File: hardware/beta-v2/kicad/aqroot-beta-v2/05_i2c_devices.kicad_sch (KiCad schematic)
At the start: 9 parts, among them U4 BMI270

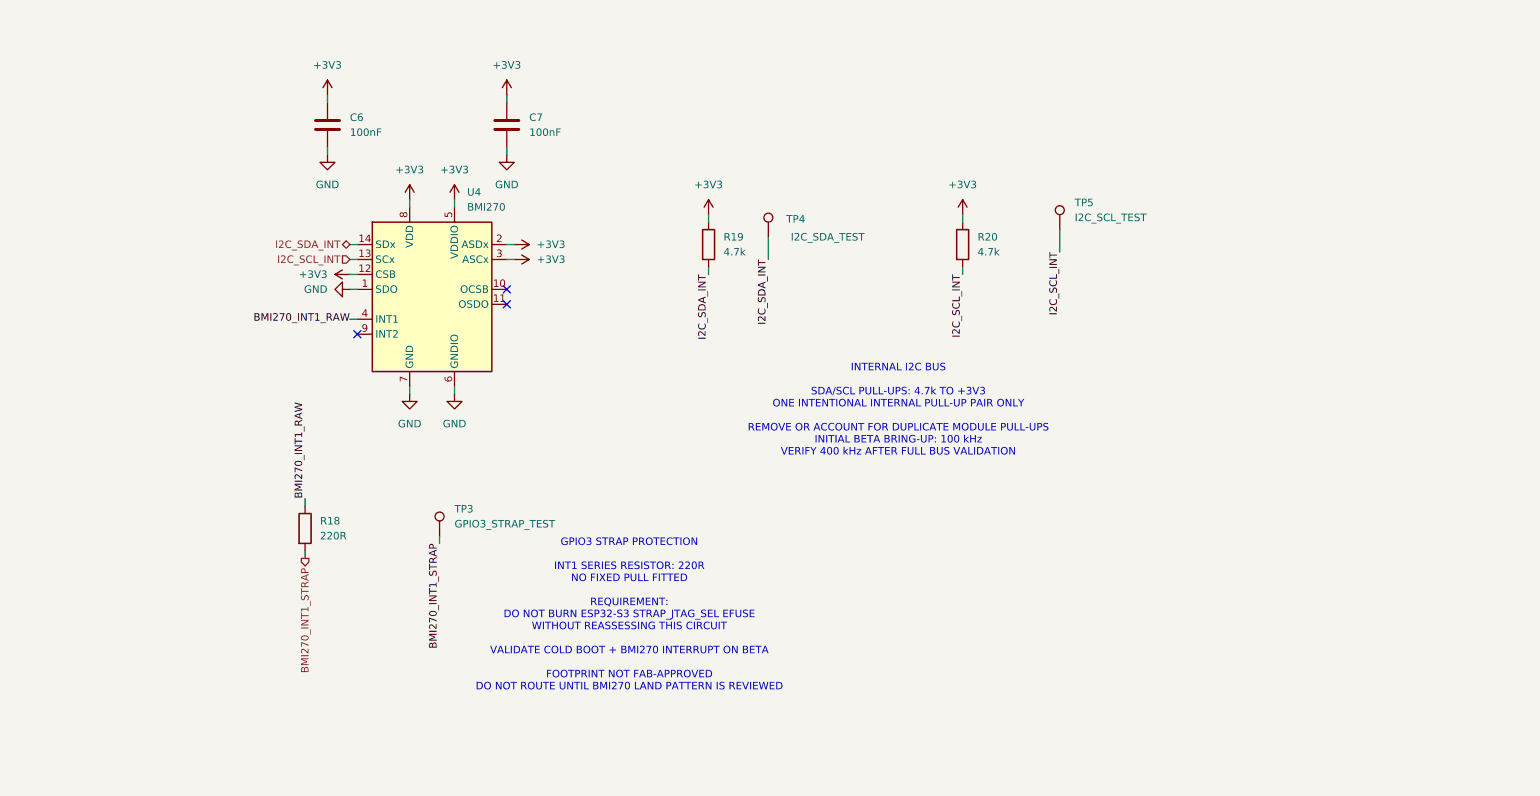
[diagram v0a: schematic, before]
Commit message: hardware: migrate Full Beta v2 I2C devices and IMU (FBV2-S1-005)
Sheet 05. Task gate FBV2-S1-I2C-IMU = PASS.
ERC 46 -> 45: zero added, one removed. Errors remain 2, both inherited.

A REPORTED NUMBER HAD TO BE CORRECTED FIRST.

FBV2-S1-004, 004B and 004C all quote "ERC 68". The stored reports say 46 -
2 errors, 44 warnings, three times over. The deltas those tasks reported
("zero added, zero removed") are correct and reproducible from the files; only
the absolute figure was wrong, and it was carried for three tasks. Sheet 04's
migration genuinely took the count from 64 to 46.

There is also a flag trap worth writing down: kicad-cli sch erc --severity-all
counts Exclusions as well and reports 104 on the same unmodified design. Every
figure in this programme is --severity-error --severity-warning, matching the
reports' own "Report includes: Errors, Warnings" header. Compare like with like
or the gate is meaningless.

NOTHING ON THIS SHEET WAS WRONG, AND THAT IS THE HONEST HEADLINE.

The brief said not to copy Beta-DM's BMI270 straps blindly. Every one was
re-derived from BST-BMI270-DS000-08 Rev 1.6:

  pin 1  SDO  -> GND    "the default I2C address ... 0b1101000 (0x68) ... if
                        the SDO pin is pulled to GND"
  pin 12 CSB  -> VDDIO  "it is recommended to hard-wire the CSB line to VDDIO"
  pin 2  ASDx -> VDDIO  "can be connected to VDDIO or left unconnected.
  pin 3  ASCx -> VDDIO   Do not connect to GND."
  pin 9  INT2 -> DNC    "If INT1 and/or INT2 are not used, please do not
  pin 10 OCSB -> DNC     connect them (DNC)."
  pin 11 OSDO -> DNC
  C6/C7 100nF at pins 5 and 8, exactly as recommended

They were all already correct. B-44 CLOSED: pad drive is IOH/IOL <= 2 mA with
VOH >= 0.8*VDDIO, against a 323 uA load - 6x margin.

THE REAL DEFECT WAS ON THE BUS.

The internal I2C bus was measured from the netlist rather than assumed - two
expanders, the IMU, the fuel gauge, the TCA9517A A-side, the touch controller
through the 50-pin display flex, two t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
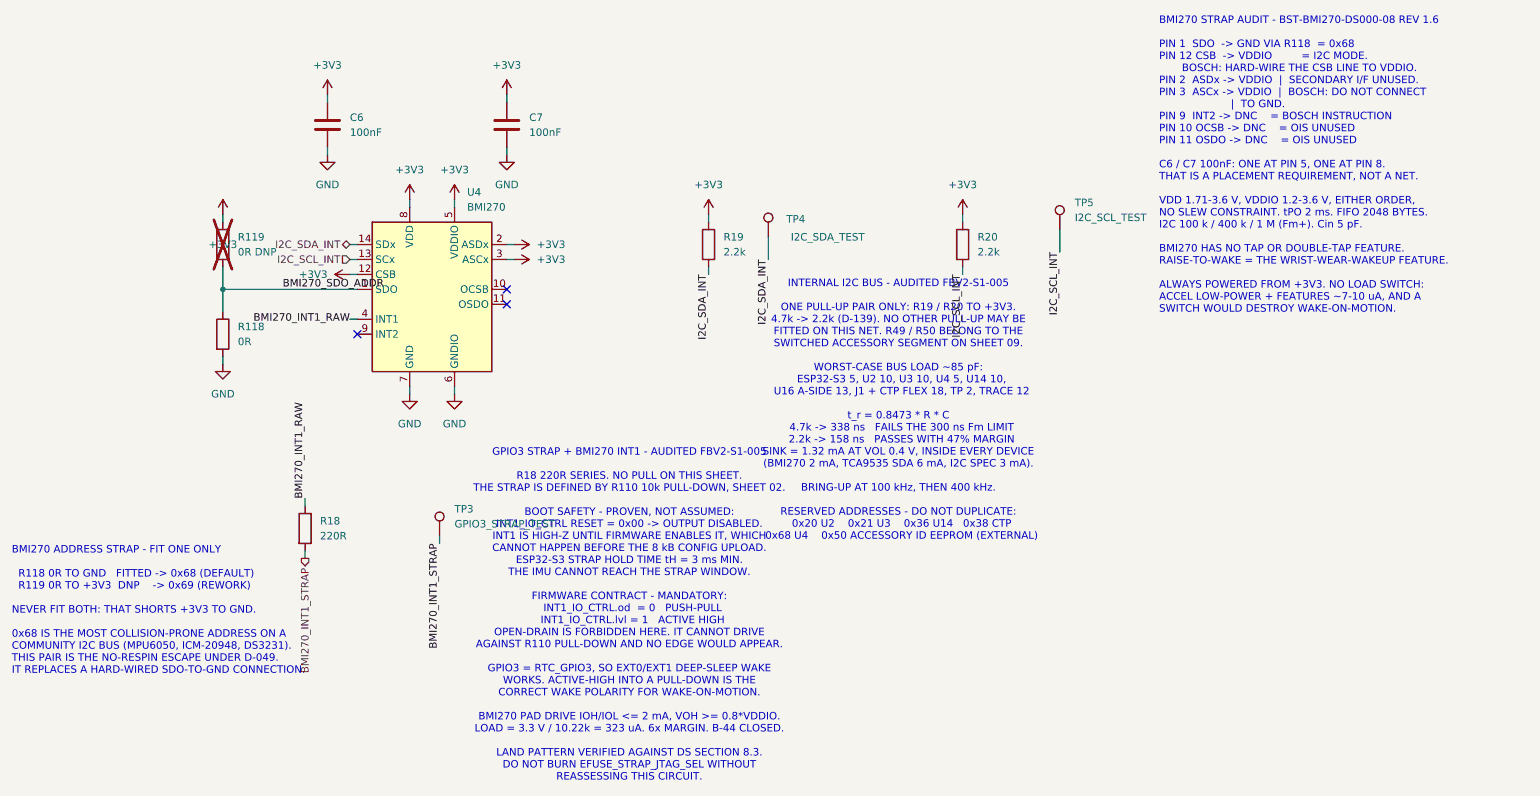
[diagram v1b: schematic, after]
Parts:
- added R118: 0R, Resistor_SMD:R_0603_1608Metric, symbol Device:R
- added R119: 0R DNP, Resistor_SMD:R_0603_1608Metric, symbol Device:R
- R19, R20: value 4.7k -> 2.2k
- U4: Note (none) -> Verified against BST-BMI270-DS000-08 Rev 1.6 (March 2026) i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
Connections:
- net +3V3: now also R119.1
- net GND: now also R118.2; no longer U4.1 (SDO)
- new net BMI270_SDO_ADDR: R118.1, R119.2, U4.1 (SDO)
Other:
- note added: "BMI270 ADDRESS STRAP - FIT ONE ONLY R118 0R TO GND FITTED -> 0x68 (DEFAULT) R119 0R TO +3V3 DNP -> 0x69 (REWORK) NEVER FIT BOTH: THAT SHORTS +3V3 TO GND. 0x68 IS THE MOST COLLISION-PRONE ADDRESS ON A COMMUNITY I2C BUS (MPU6050, ICM-20948, DS3231). THIS PAIR IS THE NO-RESPIN ESCAPE UNDER D-049. IT REPLACES A HARD-WIRED SDO-TO-GND CONNECTION."
- note added: "BMI270 STRAP AUDIT - BST-BMI270-DS000-08 REV 1.6 PIN 1 SDO -> GND VIA R118 = 0x68 PIN 12 CSB -> VDDIO = I2C MODE. BOSCH: HARD-WIRE THE CSB LINE TO VDDIO. PIN 2 ASDx -> VDDIO | SECONDARY I/F UNUSED. PIN 3 ASCx -> VDDIO | BOSCH: DO NOT CONNECT | TO GND. PIN 9 INT2 -> DNC = BOSCH INSTRUCTION PIN 10 OCSB -> DNC = OIS UNUSED PIN 11 OSDO -> DNC = OIS UNUSED C6 / C7 100nF: ONE AT PIN 5, ONE AT PIN 8. TH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"
- note added: "GPIO3 STRAP + BMI270 INT1 - AUDITED FBV2-S1-005 R18 220R SERIES. NO PULL ON THIS SHEET. THE STRAP IS DEFINED BY R110 10k PULL-DOWN, SHEET 02. BOOT SAFETY - PROVEN, NOT ASSUMED: INT1_IO_CTRL RESET = 0x00 -> OUTPUT DISABLED. INT1 IS HIGH-Z UNTIL FIRMWARE ENABLES IT, WHICH CANNOT HAPPEN BEFORE THE 8 kB CONFIG UPLOAD. ESP32-S3 STRAP HOLD TIME tH = 3 ms MIN. THE IMU CANNOT REACH THE STRAP WINDOW. FIRM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"
- note added: "INTERNAL I2C BUS - AUDITED FBV2-S1-005 ONE PULL-UP PAIR ONLY: R19 / R20 TO +3V3. 4.7k -> 2.2k (D-139). NO OTHER PULL-UP MAY BE FITTED ON THIS NET. R49 / R50 BELONG TO THE SWITCHED ACCESSORY SEGMENT ON SHEET 09. WORST-CASE BUS LOAD ~85 pF: ESP32-S3 5, U2 10, U3 10, U4 5, U14 10, U16 A-SIDE 13, J1 + CTP FLEX 18, TP 2, TRACE 12 t_r = 0.8473 * R * C 4.7k -> 338 ns FAILS THE 300 ns Fm LIMIT 2.2k -> 15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"
- note removed: "GPIO3 STRAP PROTECTION INT1 SERIES RESISTOR: 220R NO FIXED PULL FITTED REQUIREMENT: DO NOT BURN ESP32-S3 STRAP_JTAG_SEL EFUSE WITHOUT REASSESSING THIS CIRCUIT VALIDATE COLD BOOT + BMI270 INTERRUPT ON BETA FOOTPRINT NOT FAB-APPROVED DO NOT ROUTE UNTIL BMI270 LAND PATTERN IS REVIEWED"
- note removed: "INTERNAL I2C BUS SDA/SCL PULL-UPS: 4.7k TO +3V3 ONE INTENTIONAL INTERNAL PULL-UP PAIR ONLY REMOVE OR ACCOUNT FOR DUPLICATE MODULE PULL-UPS INITIAL BETA BRING-UP: 100 kHz VERIFY 400 kHz AFTER FULL BUS VALIDATION"

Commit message: hardware: close Full Beta v2 S2 release blockers
Closes B-03, B-63, B-70 and B-71's schematic-side work. Property-only
changes to the nine sheets plus the microphone footprint; ERC unchanged
at 27 / 0 errors / 27 with an identical violation histogram, and the PCB
is untouched and still bit-identical to Beta-DM.

B-03 - all eight remaining Tier-2 footprints compared dimension by
dimension against retrieved manufacturer drawings. Y1 moves from
candidate to lock (Yajingxin TXM27.12M0004322DBBDO00T, C362365, 3421 in
stock) with a land that matches the vendor's Suggested Layout exactly.
The MAX98357A looked like a genuine defect - outline 21-0136 gives
T1633-5 an EP of 1.50/1.60/1.70 while the land is 1.23 - and is not:
land pattern 90-0032 Rev E is issued for T1633-5, -5C and -7C together
and specifies one land for all three, so no project-local footprint was
created.

B-63 - the microphone acoustic port is now drawn rather than described.
1.05 mm NPTH taken from the drawing's own pad-4 ring inner diameter,
paste pulled back 0.10 mm as a declared stencil choice, keepout marked,
bottom-port orientation recorded.

B-70 - L5/L6 lock to Murata LQW18AN39NG80D. The DCR is a first-order
term here: 0.20 ohm max against R_q = 1.1 ohm drops network Q from 25.3
to about 21.4, so the antenna must be tuned with this exact part fitted
and the first lever is R_q, not 39 nH.

B-71 - 65 LCSC fields written in, three MPN strings corrected. J6 and J7
carried bare order codes that resolve to zero-stock listings while the
plating-suffixed strings are abundantly stocked. Six substitution traps
recorded in the symbols themselves, including BAT54W offered for
BAT54WS - a single diode for a series pair - and a clone for the battery
reverse-polarity pass FETs.

Eight DNP parts still carried no recorded reason and now do. The design
has zero unexplained DNP.

Co-Authored-By: Claude Opus 5 <noreply@anthropic.com>
Claude-Session: https://claude.ai/code/session_0133CdFHfKcCH8oPWqJZWe7o
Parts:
- R119: Note2 (none) -> DNP BY DESIGN - documented 2026-08-23 (FBV2-S2-002). R119 i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
- U4: LCSC (none) -> C2836813
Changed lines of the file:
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@@
+			)
+		)
+		(property "LCSC" "C2836813"
+			(at 91.44 87.63 0)
+			(hide yes)
+			(show_name no)
+			(do_not_autoplace no)
+			(effects
+				(font
+					(size 1.27 1.27)
+				)
 			)
 		)
@@
 			(at 55.88 78.74 0)
 			(hide yes)
+			(show_name no)
+			(do_not_autoplace no)
+			(effects
+				(font
+					(size 1.27 1.27)
+				)
+			)
+		)
+		(property "Note2" "DNP BY DESIGN - documented 2026-08-23 (FBV2-S2-002). R119 is the ALTERNATE-ADDRESS strap for the BMI270: it would pull BMI270_SDO_ADDR up to +3V3. R118 (FITTED, 0 R to GND) holds the strap LOW, so the IMU answers at 0x68, which is what I2C_ADDRESS_REGISTRY.md records. R118 and R119 ARE MUTUALLY EXCLUSIVE - fitting both shorts +3V3 to GND through two 0 R resistors. This pair is a no-respin address escape under D-049 in case of a future address collision. It had no note at all before FBV2-S2-002."
+			(at 55.88 78.74 0)
+			(hide yes)
